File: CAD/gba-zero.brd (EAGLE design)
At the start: 130.7 x 72.9 mm, 57 parts, among them IC5 APX803, Q2 BSS138, U1 NC7WZ16, U2 LM4875

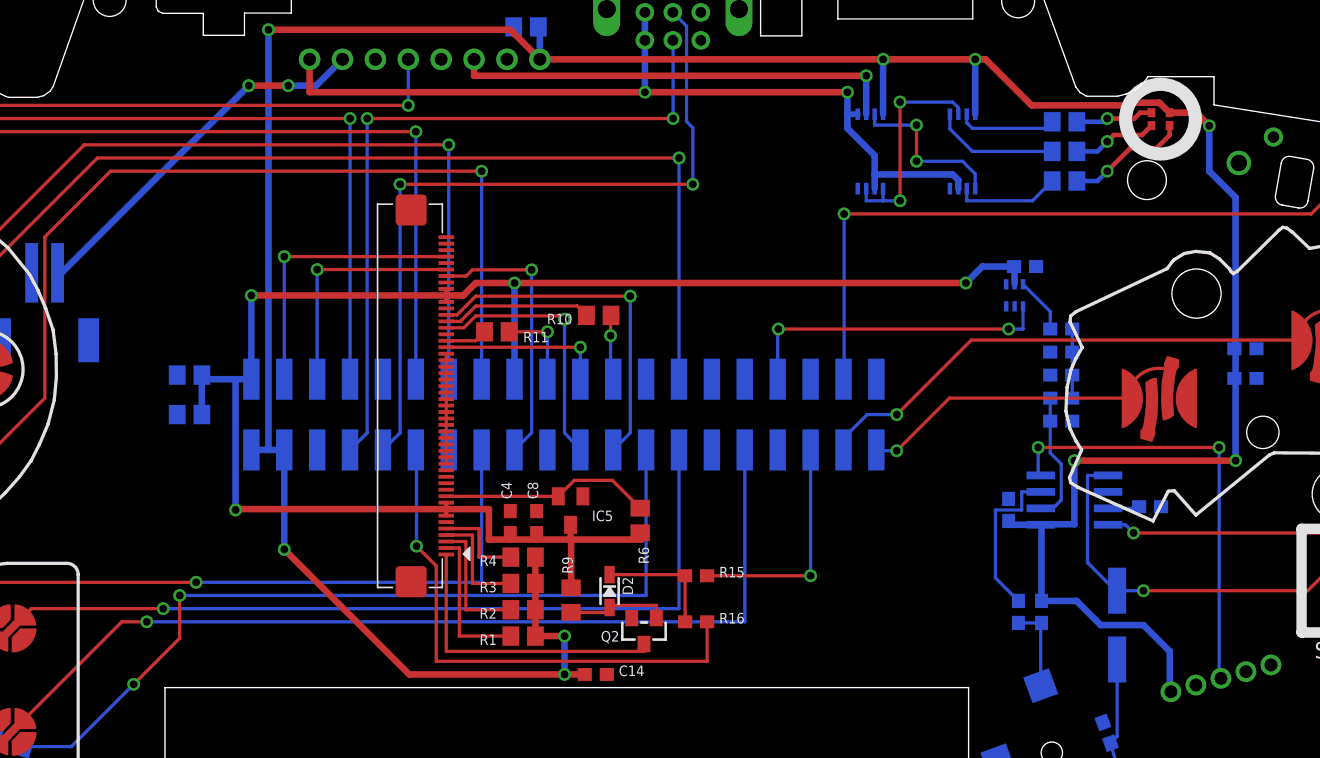
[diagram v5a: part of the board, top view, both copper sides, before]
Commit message: Final board tweaks Added DRU file
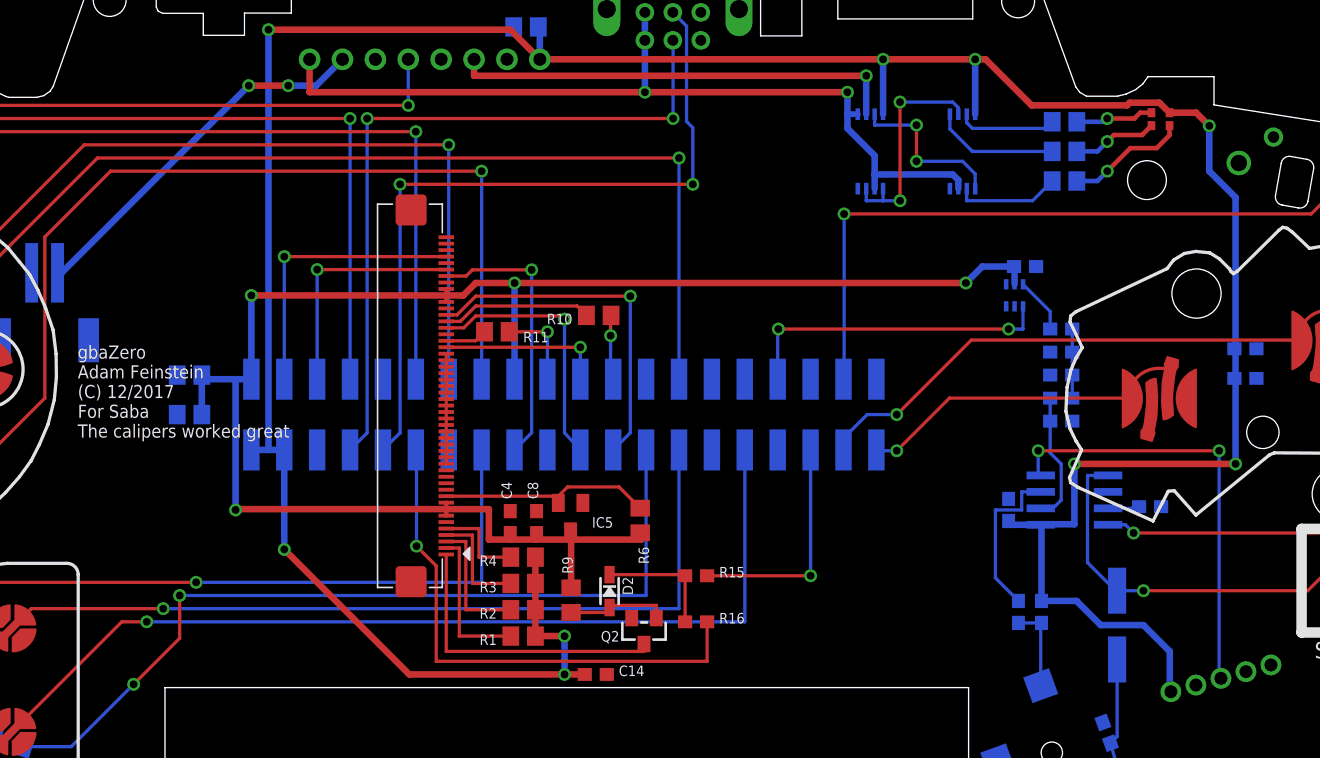
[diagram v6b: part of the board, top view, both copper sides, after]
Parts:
- moved IC5 0.51 mm to (67.5, 30.7)
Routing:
- net VOL/SD: track 34.2 -> 33.7 mm
- net 3.3V: track 134.4 -> 133.9 mm
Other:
- board text added: "gbaZero Adam Feinstein (C) 12/2017 For Saba The calipers worked great"
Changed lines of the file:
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@@
 <hole x="126.78759375" y="32.478265625" drill="4"/>
 <hole x="6.13759375" y="28.588890625" drill="4"/>
-<circle x="113.0755" y="61.42" radius="2.6924" width="1.016" layer="21"/>
+<circle x="113.0755" y="61.42" radius="2.6924" width="1.016" layer="51"/>
 <circle x="112.029784375" y="56.711425" radius="3.3528" width="0.0127" layer="22"/>
 <circle x="21.69509375" y="56.767015625" radius="3.3528" width="0.0127" layer="22"/>
 <wire x1="36.203840625" y1="17.526" x2="36.203840625" y2="7.68698125" width="0" layer="20"/>
 <wire x1="98.2533625" y1="17.526" x2="36.203840625" y2="17.526" width="0" layer="20"/>
+<text x="29.464" y="36.83" size="1.016" layer="25" font="vector">gbaZero
+Adam Feinstein
+(C) 12/2017
+For Saba
+The calipers worked great</text>
 </plain>
 <attributes>
@@
 <element name="C1" library="microbuilder" package="0805" value="10uF" x="38.1" y="38.608" rot="MR0"/>
 <element name="C5" library="microbuilder" package="0805" value="10uF" x="64.081659375" y="68.539359375" rot="MR0"/>
-<element name="IC5" library="adafruit" package="SOT23" value="APX803" x="67.523359375" y="31.193740625" smashed="yes" rot="R180">
-<attribute name="NAME" x="69.174359375" y="31.193740625" size="0.8128" layer="25" font="vector" ratio="18" rot="R180" align="bottom-right"/>
-<attribute name="VALUE" x="69.174359375" y="31.828740625" size="0.4064" layer="27" font="vector" ratio="10" rot="R180" align="bottom-right"/>
+<element name="IC5" library="adafruit" package="SOT23" value="APX803" x="67.523359375" y="30.685740625" smashed="yes" rot="R180">
+<attribute name="NAME" x="69.174359375" y="30.685740625" size="0.8128" layer="25" font="vector" ratio="18" rot="R180" align="bottom-right"/>
+<attribute name="VALUE" x="69.174359375" y="31.320740625" size="0.4064" layer="27" font="vector" ratio="10" rot="R180" align="bottom-right"/>
 </element>
 <element name="U$2" library="gba-zero-parts" package="FPC-50-CON" value="50_PIN_CON" x="55.2704" y="40.0558" locked="yes" smashed="yes" rot="R270"/>
@@
 <contactref element="U$2" pad="10"/>
 <wire x1="57.9204" y1="32.3058" x2="57.9204" y2="32.293740625" width="0.254" layer="1"/>
-<wire x1="57.9204" y1="32.293740625" x2="66.573359375" y2="32.293740625" width="0.254" layer="1"/>
-<wire x1="72.898" y1="31.381740625" x2="70.751740625" y2="33.528" width="0.254" layer="1"/>
-<wire x1="70.751740625" y1="33.528" x2="67.80761875" y2="33.528" width="0.254" layer="1"/>
-<wire x1="67.80761875" y1="33.528" x2="66.573359375" y2="32.293740625" width="0.254" layer="1"/>
+<wire x1="57.9204" y1="32.3058" x2="66.573359375" y2="32.3058" width="0.254" layer="1"/>
+<wire x1="66.573359375" y1="32.3058" x2="66.573359375" y2="31.785740625" width="0.254" layer="1"/>
+<wire x1="72.898" y1="31.381740625" x2="71.259740625" y2="33.02" width="0.254" layer="1"/>
+<wire x1="71.259740625" y1="33.02" x2="67.287559375" y2="33.02" width="0.254" layer="1"/>
+<wire x1="67.287559375" y1="33.02" x2="66.573359375" y2="32.3058" width="0.254" layer="1"/>
 </signal>
 <signal name="RT_INT">
@@
 <wire x1="67.523359375" y1="28.956" x2="64.897" y2="28.956" width="0.508" layer="1"/>
 <wire x1="64.897" y1="28.956" x2="62.865" y2="28.956" width="0.508" layer="1"/>
-<wire x1="67.523359375" y1="30.093740625" x2="67.523359375" y2="28.956" width="0.508" layer="1"/>
+<wire x1="67.523359375" y1="29.585740625" x2="67.523359375" y2="28.956" width="0.508" layer="1"/>
 <wire x1="57.9204" y1="31.3058" x2="41.656" y2="31.3058" width="0.508" layer="1"/>
 <wire x1="41.656" y1="31.3058" x2="41.656" y2="31.242" width="0.508" layer="1"/>
@@
 <wire x1="113.792" y1="17.290459375" x2="113.877996875" y2="17.2044625" width="0.508" layer="16"/>
 <wire x1="118.872" y1="43.776" x2="118.784" y2="43.688" width="0.508" layer="16"/>
-<wire x1="106.426" y1="30.138" x2="106.426" y2="35.052" width="0.508" layer="16"/>
-<via x="106.426" y="35.052" extent="1-16" drill="0.6" shape="square"/>
-<wire x1="106.426" y1="35.052" x2="118.872" y2="35.052" width="0.508" layer="1"/>
-<via x="118.872" y="35.052" extent="1-16" drill="0.6" shape="square"/>
-<wire x1="118.872" y1="35.052" x2="118.872" y2="41.402" width="0.508" layer="16"/>
+<wire x1="106.426" y1="30.138" x2="106.426" y2="34.798" width="0.508" layer="16"/>
+<via x="106.426" y="34.798" extent="1-16" drill="0.6" shape="square"/>
+<wire x1="106.426" y1="34.798" x2="118.872" y2="34.798" width="0.508" layer="1"/>
+<via x="118.872" y="34.798" extent="1-16" drill="0.6" shape="square"/>
+<wire x1="118.872" y1="34.798" x2="118.872" y2="41.402" width="0.508" layer="16"/>
 <wire x1="106.426" y1="30.138" x2="103.865" y2="30.138" width="0.508" layer="16"/>
 <wire x1="103.865" y1="30.138" x2="103.826" y2="30.099" width="0.508" layer="16"/>
@@
 <contactref element="U2" pad="4"/>
 <wire x1="117.7417" y1="18.239740625" x2="117.602" y2="18.239740625" width="0.254" layer="16"/>
-<wire x1="117.602" y1="18.239740625" x2="117.602" y2="36.068" width="0.254" layer="16"/>
-<via x="117.602" y="36.068" extent="1-16" drill="0.6" shape="square"/>
-<wire x1="117.602" y1="36.068" x2="103.632" y2="36.068" width="0.254" layer="1"/>
-<via x="103.632" y="36.068" extent="1-16" drill="0.6" shape="square"/>
-<wire x1="103.632" y1="36.068" x2="103.632" y2="34.103" width="0.254" layer="16"/>
+<wire x1="117.602" y1="18.239740625" x2="117.602" y2="35.814" width="0.254" layer="16"/>
+<via x="117.602" y="35.814" extent="1-16" drill="0.6" shape="square"/>
+<wire x1="117.602" y1="35.814" x2="103.632" y2="35.814" width="0.254" layer="1"/>
+<via x="103.632" y="35.814" extent="1-16" drill="0.6" shape="square"/>
+<wire x1="103.632" y1="35.814" x2="103.632" y2="34.103" width="0.254" layer="16"/>
 <wire x1="103.632" y1="34.103" x2="103.826" y2="33.909" width="0.254" layer="16"/>
 </signal>
@@
 </board>
 </drawing>
+<compatibility>
+<note version="6.3" minversion="6.2.2" severity="warning">
+Since Version 6.2.2 text objects can contain more than one line,
+which will not be processed correctly with this version.
+</note>
+</compatibility>
 </eagle>
